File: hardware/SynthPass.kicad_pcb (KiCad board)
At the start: 4 copper layers, 19.1 x 16.8 mm, 17 parts, among them J1 SM04B-SRSS-TB, P1 USB_C_Plug_USB2.0, SW1 SW_Push, U2 CH572D, Y2 32MHz

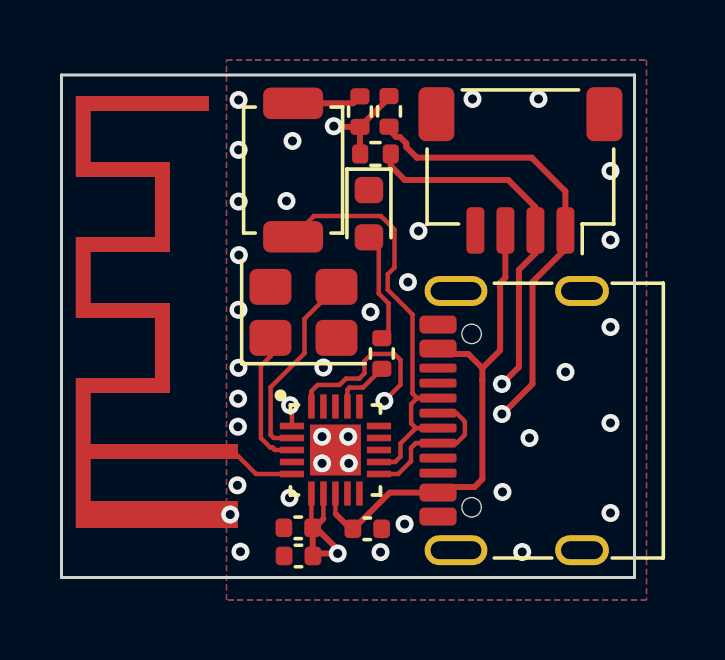
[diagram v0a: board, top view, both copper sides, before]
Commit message: Change CH572 symbol, change UDP resistor to 1K5, add 1K5 5V->3V3 resistor
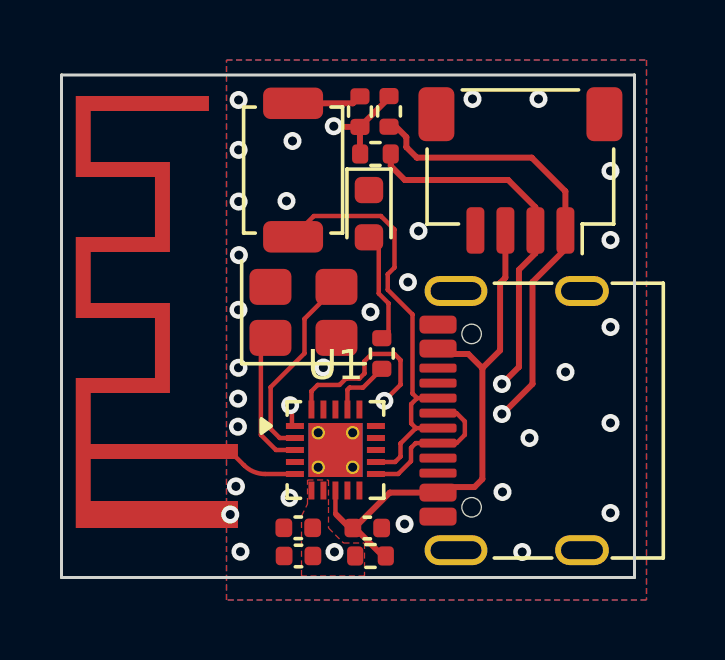
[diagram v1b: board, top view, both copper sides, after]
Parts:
- removed U2: CH572D, CH572D:CH572D
- added R5: 1K5, Resistor_SMD:R_0402_1005Metric, F.Cu at (159.8, 65.5)
- added U1: CH572D, CH572D:CH572D_New, F.Cu at (158.6, 62.0)
- AE1: value PCB Antenna -> SWRA117D
- J2: renamed from P1; value USB_C_Plug_USB2.0 -> USB_C_Receptacle_USB2.0_16P
- R1: value 5.1k -> 1K5
- renumbered Y2 to Y1
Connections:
- net UDM renamed UDN
- AE1 pad 1: Net-(AE1-FEED) -> /ANT
- J2 pad A8: (no net) -> unconnected-(J2-SBU1-PadA8)
- J2 pad B8: (no net) -> unconnected-(J2-SBU2-PadB8)
- J2 pad SH: (no net) -> GND
- Y1 pad 1: Net-(U2-XI) -> /XI
- Y1 pad 3: Net-(U2-XO) -> /XO
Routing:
- net Net-(U2-XO): track 6.59 -> 0.00 mm
- net /XO: track 0.00 -> 6.48 mm
- net +3V3: track 8.77 -> 3.15 mm
- net Net-(U2-XI): track 4.68 -> 0.00 mm
- net /XI: track 0.00 -> 4.16 mm
- net /ANT: track 0.00 -> 2.42 mm
- net Net-(AE1-FEED): track 2.37 -> 0.00 mm
- net VBUS: track 16.9 -> 17.7 mm
- net SCL: track 23.7 -> 22.9 mm
- net GND: track 0.22 -> 0.00 mm, vias 35 -> 30
- added copper zone on F.Cu, net +3V3
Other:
- board text added: "R1.1"
- board text removed: "R1"
